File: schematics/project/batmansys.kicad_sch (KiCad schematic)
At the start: 0 parts

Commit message: some progress, dust slowly clears
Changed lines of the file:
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@@
 (kicad_sch (version 20211123) (generator eeschema)
   (paper "A4")
+  (bus_alias "RS485_BMS" (members "RS485_A" "RS485_B"))
+  (bus_entry (at 153.67 52.07) (size -2.54 2.54)
+    (stroke (width 0) (type default) (color 0 0 0 0))
+  )
+  (bus_entry (at 153.67 54.61) (size -2.54 2.54)
+    (stroke (width 0) (type default) (color 0 0 0 0))
+  )
+  (bus (pts (xy 171.45 52.07) (xy 153.67 52.07))
+    (stroke (width 0) (type default) (color 0 0 0 0))
+  )
+  (wire (pts (xy 132.08 54.61) (xy 151.13 54.61))
+    (stroke (width 0) (type default) (color 0 0 0 0))
+  )
+  (bus (pts (xy 153.67 52.07) (xy 153.67 54.61))
+    (stroke (width 0) (type default) (color 0 0 0 0))
+  )
+  (wire (pts (xy 132.08 57.15) (xy 151.13 57.15))
+    (stroke (width 0) (type default) (color 0 0 0 0))
+  )
   (text "- RS485/Can to communicate with teensy\n- connect ntc\n\n- UART to bluetooth?\n- Light board port?"
     (at 105.41 87.63 0)
     (effects (font (size 1.27 1.27)) (justify left bottom))
   )
+  (label "{RS485_BMS}" (at 156.21 52.07 0)
+    (effects (font (size 1.27 1.27)) (justify left bottom))
+  )
+  (label "RS485_A" (at 132.08 54.61 0)
+    (effects (font (size 1.27 1.27)) (justify left bottom))
+  )
+  (label "RS485_B" (at 132.08 57.15 0)
+    (effects (font (size 1.27 1.27)) (justify left bottom))
+  )

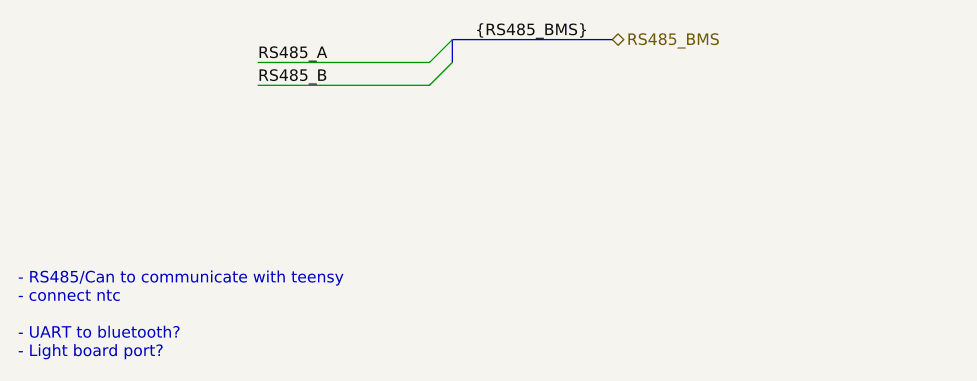
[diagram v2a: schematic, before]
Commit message: Adding separate library, BT Module
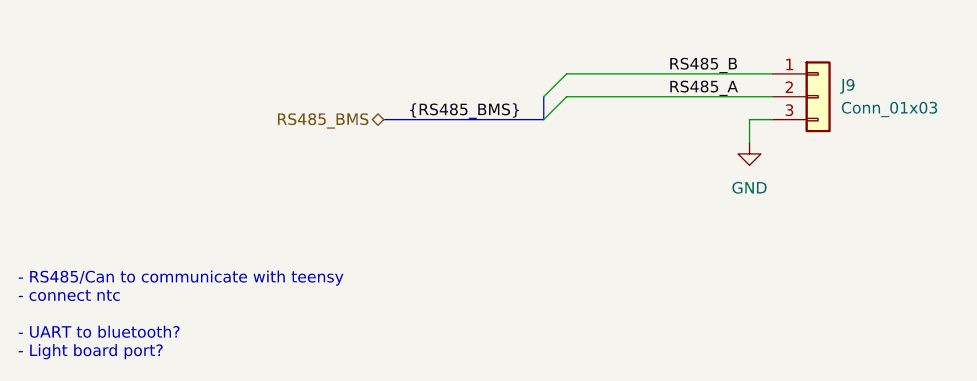
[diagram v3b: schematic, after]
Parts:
- added J9: Conn_01x03, symbol Connector_Generic:Conn_01x03
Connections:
- net RS485_A: now also J9.2 (Pin_2)
- net RS485_B: now also J9.1 (Pin_1)
- new net GND: J9.3 (Pin_3)
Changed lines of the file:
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@@
   (paper "A4")
   (bus_alias "RS485_BMS" (members "RS485_A" "RS485_B"))
-  (bus_entry (at 153.67 52.07) (size -2.54 2.54)
+  (bus_entry (at 163.83 60.96) (size 2.54 -2.54)
     (stroke (width 0) (type default) (color 0 0 0 0))
   )
-  (bus_entry (at 153.67 54.61) (size -2.54 2.54)
+  (bus_entry (at 163.83 58.42) (size 2.54 -2.54)
     (stroke (width 0) (type default) (color 0 0 0 0))
   )
-  (bus (pts (xy 171.45 52.07) (xy 153.67 52.07))
+  (wire (pts (xy 166.37 55.88) (xy 189.23 55.88))
     (stroke (width 0) (type default) (color 0 0 0 0))
   )
-  (wire (pts (xy 132.08 54.61) (xy 151.13 54.61))
+  (bus (pts (xy 146.05 60.96) (xy 163.83 60.96))
     (stroke (width 0) (type default) (color 0 0 0 0))
   )
-  (bus (pts (xy 153.67 52.07) (xy 153.67 54.61))
+  (wire (pts (xy 166.37 58.42) (xy 189.23 58.42))
     (stroke (width 0) (type default) (color 0 0 0 0))
   )
-  (wire (pts (xy 132.08 57.15) (xy 151.13 57.15))
+  (bus (pts (xy 163.83 60.96) (xy 163.83 58.42))
+    (stroke (width 0) (type default) (color 0 0 0 0))
+  )
+  (wire (pts (xy 186.69 60.96) (xy 189.23 60.96))
+    (stroke (width 0) (type default) (color 0 0 0 0))
+  )
+  (wire (pts (xy 186.69 63.5) (xy 186.69 60.96))
     (stroke (width 0) (type default) (color 0 0 0 0))
   )
@@
     (effects (font (size 1.27 1.27)) (justify left bottom))
   )
-  (label "{RS485_BMS}" (at 156.21 52.07 0)
-    (effects (font (size 1.27 1.27)) (justify left bottom))
+  (label "{RS485_BMS}" (at 161.29 60.96 180)
+    (effects (font (size 1.27 1.27)) (justify right bottom))
   )
-  (label "RS485_A" (at 132.08 54.61 0)
-    (effects (font (size 1.27 1.27)) (justify left bottom))
+  (label "RS485_A" (at 185.42 58.42 180)
+    (effects (font (size 1.27 1.27)) (justify right bottom))
   )
-  (label "RS485_B" (at 132.08 57.15 0)
-    (effects (font (size 1.27 1.27)) (justify left bottom))
+  (label "RS485_B" (at 185.42 55.88 180)
+    (effects (font (size 1.27 1.27)) (justify right bottom))
   )
-  (hierarchical_label "RS485_BMS" (shape bidirectional) (at 171.45 52.07 0)
-    (effects (font (size 1.27 1.27)) (justify left))
+  (hierarchical_label "RS485_BMS" (shape bidirectional) (at 146.05 60.96 180)
+    (effects (font (size 1.27 1.27)) (justify right))
+  )
+  (symbol (lib_id "power:GND") (at 186.69 63.5 0) (unit 1)
+    (in_bom yes) (on_board yes) (fields_autoplaced)
+    (property "Reference" "#PWR08" (id 0) (at 186.69 69.85 0)
+      (effects (font (size 1.27 1.27)) hide)
+    )
+    (property "Value" "GND" (id 1) (at 186.69 68.58 0))
+    (property "Footprint" "" (id 2) (at 186.69 63.5 0)
+      (effects (font (size 1.27 1.27)) hide)
+    )
+    (property "Datasheet" "" (id 3) (at 186.69 63.5 0)
+      (effects (font (size 1.27 1.27)) hide)
+    )
+    (pin "1")
+  )
+  (symbol (lib_id "Connector_Generic:Conn_01x03") (at 194.31 58.42 0) (unit 1)
+    (in_bom yes) (on_board yes) (fields_autoplaced)
+    (property "Reference" "J9" (id 0) (at 196.85 57.1499 0)
+      (effects (font (size 1.27 1.27)) (justify left))
+    )
+    (property "Value" "Conn_01x03" (id 1) (at 196.85 59.6899 0)
+      (effects (font (size 1.27 1.27)) (justify left))
+    )
+    (property "Footprint" "" (id 2) (at 194.31 58.42 0)
+      (effects (font (size 1.27 1.27)) hide)
+    )
+    (property "Datasheet" "~" (id 3) (at 194.31 58.42 0)
+      (effects (font (size 1.27 1.27)) hide)
+    )
+    (pin "1")
+    (pin "2")
+    (pin "3")
   )
 )

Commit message: random commit
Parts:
- J9: footprint (none) -> Connector_JST:JST_SH_SM03B-SRSS-TB_1x03-1MP_P1.00mm_Horizontal
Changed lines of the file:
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@@
       (effects (font (size 1.27 1.27)) (justify left))
     )
-    (property "Footprint" "" (id 2) (at 194.31 58.42 0)
+    (property "Footprint" "Connector_JST:JST_SH_SM03B-SRSS-TB_1x03-1MP_P1.00mm_Horizontal" (id 2) (at 194.31 58.42 0)
       (effects (font (size 1.27 1.27)) hide)
     )
